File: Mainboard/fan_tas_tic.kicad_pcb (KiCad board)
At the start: 2 copper layers, 155 x 175 mm, 125 parts, among them J1 Ti_Booster_40_J1, P1 CONN_01X04, P10 CONN_01X08, P11 CONN_01X04, P12 CONN_01X04, P13 CONN_01X04, P14 CONN_01X04, P2 CONN_01X04, P3 CONN_01X04, P4 CONN_01X04, P5 CONN_01X04, P6 CONN_01X08, P7 CONN_01X08, P8 CONN_01X08, P9 CONN_01X08, Q1 IRL640, Q10 IRL640, Q11 IRL640, Q12 IRL640, Q13 BSS138, Q14 BSS138, Q15 BSS138, Q16 BSS138, Q17 BSS138, Q18 BSS138, Q19 BSS138, Q2 IRL640, Q20 BSS138, Q3 IRL640, Q4 IRL640, Q5 IRL640, Q6 IRL640, Q7 IRL640, Q8 IRL640, Q9 IRL640, U1 7812, U2 7805, U3 UCC27524, U4 UCC27524, U5 TPIC6B595, U6 PCF8574

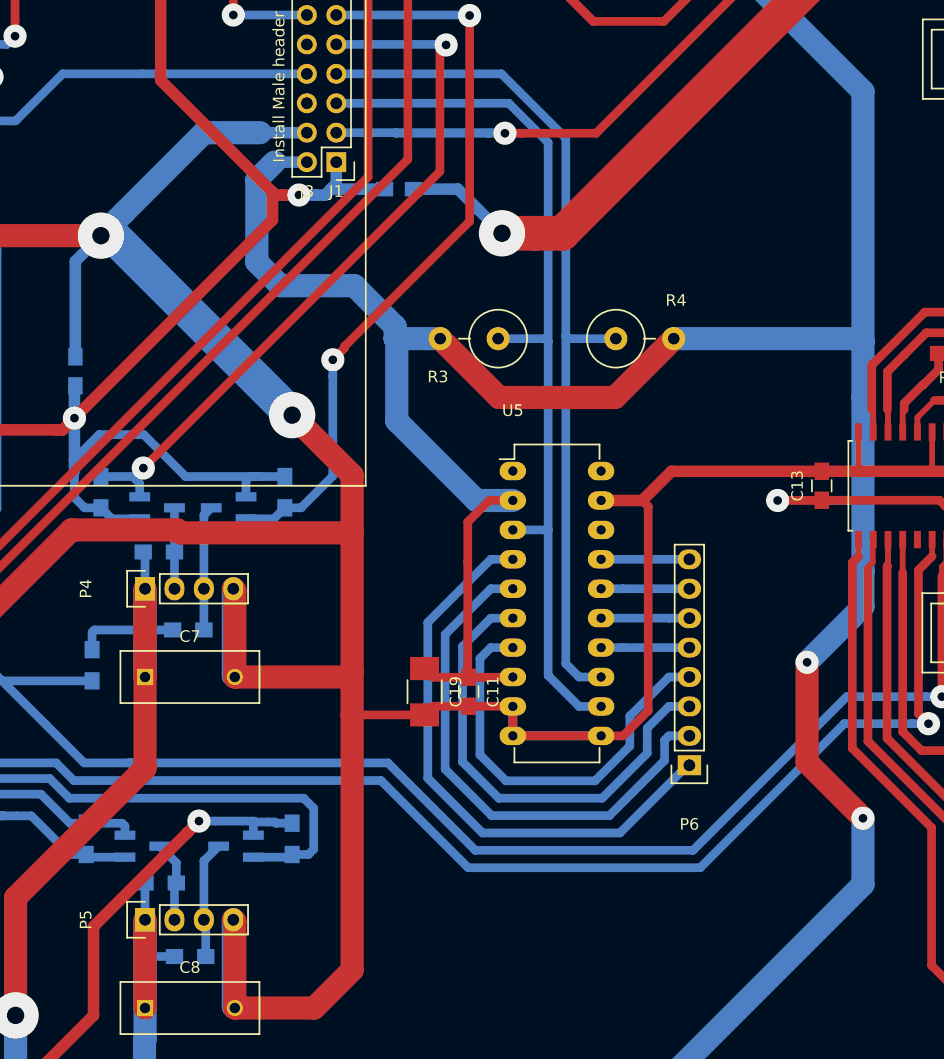
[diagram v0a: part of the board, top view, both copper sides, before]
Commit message: Made space for TM4C123 USB connector
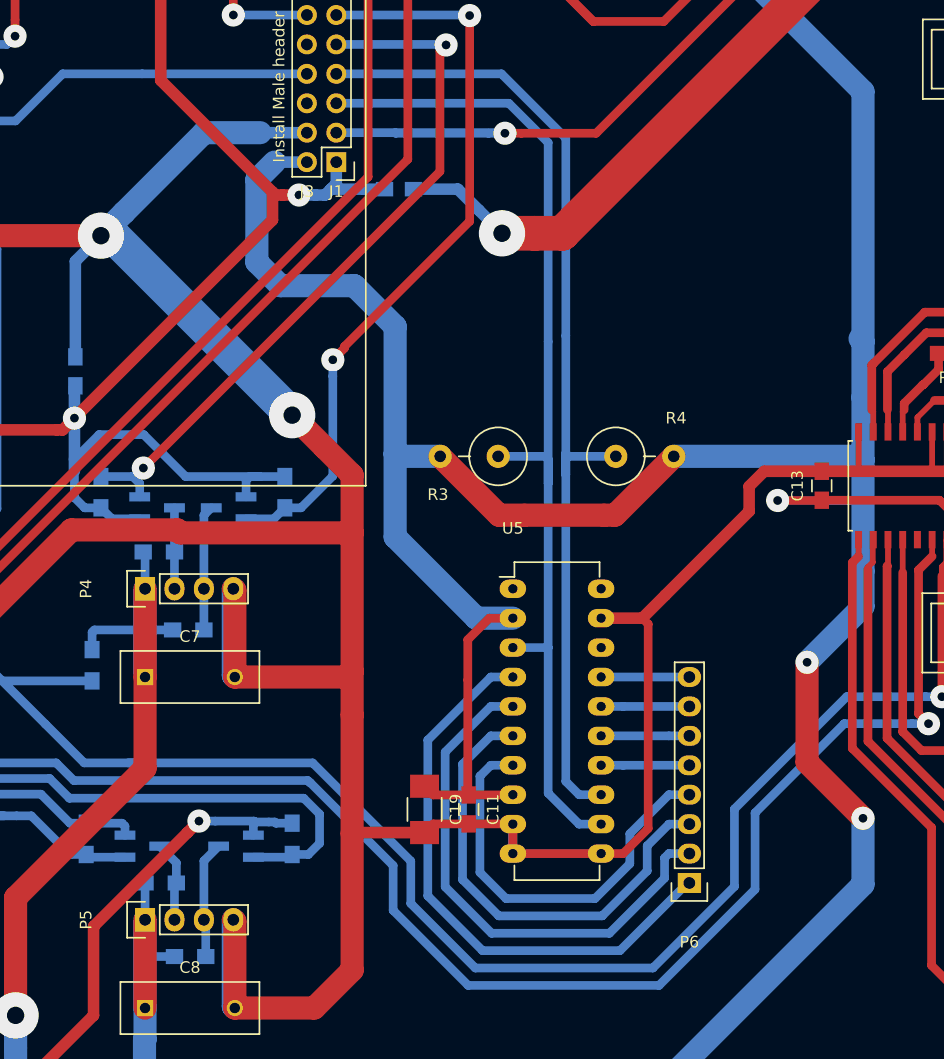
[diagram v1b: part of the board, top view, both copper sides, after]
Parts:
- moved U5 10.2 mm to (88.8, 137.6)
- moved C11 10.2 mm to (85.0, 156.7)
- moved C19 10.2 mm to (81.2, 156.7)
- moved P6 10.2 mm to (104.1, 163.0)
- moved R3 10.2 mm to (85.1, 126.2)
- moved R4 10.2 mm to (100.2, 126.2)
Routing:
- net /I2C_LEVEL_SHIFT0/A_5V: track 135.0 -> 149.6 mm
- net /I2C_LEVEL_SHIFT0/B_5V: track 140.4 -> 154.8 mm
- net /TiviaBoard/sm_col_dat: track 79.2 -> 91.4 mm
- net /TiviaBoard/sm_col_clk: track 75.8 -> 87.8 mm
- net +5V: track 690.9 -> 701.6 mm
- net GND: track 1153.4 -> 1158.9 mm

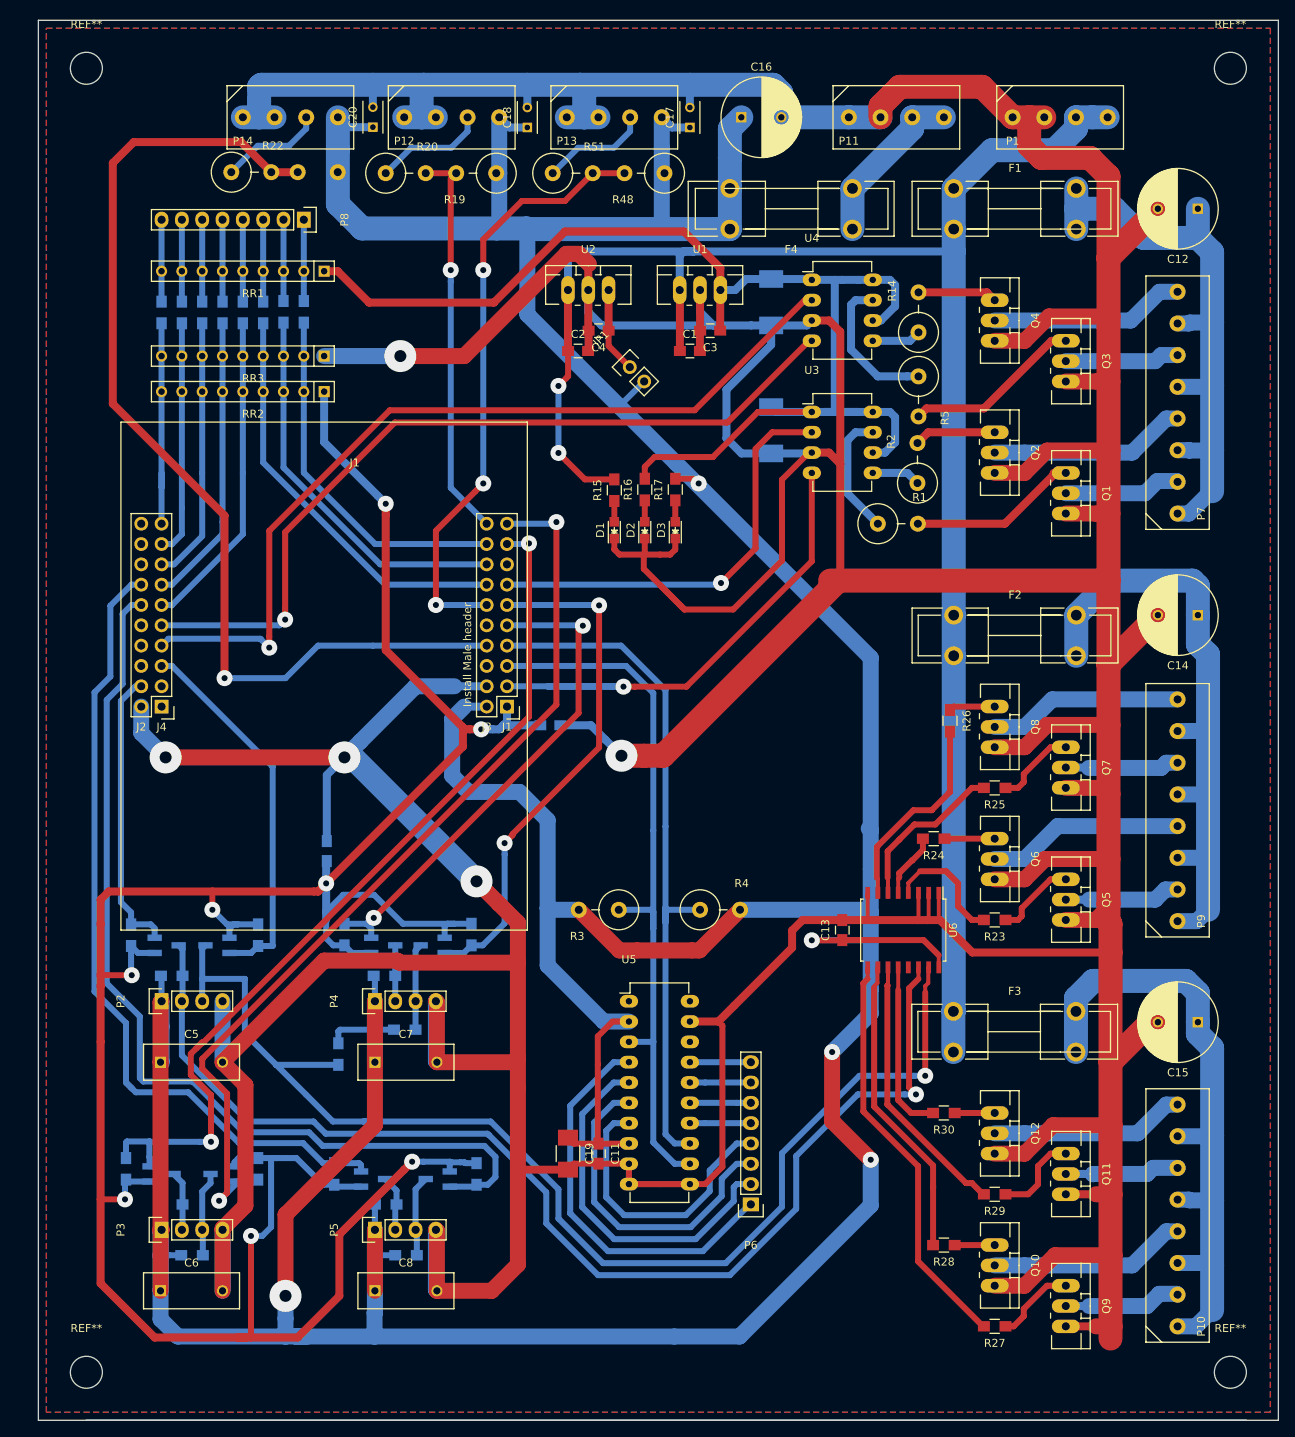
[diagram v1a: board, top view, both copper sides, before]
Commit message: Still Missing WS2811 level shifter
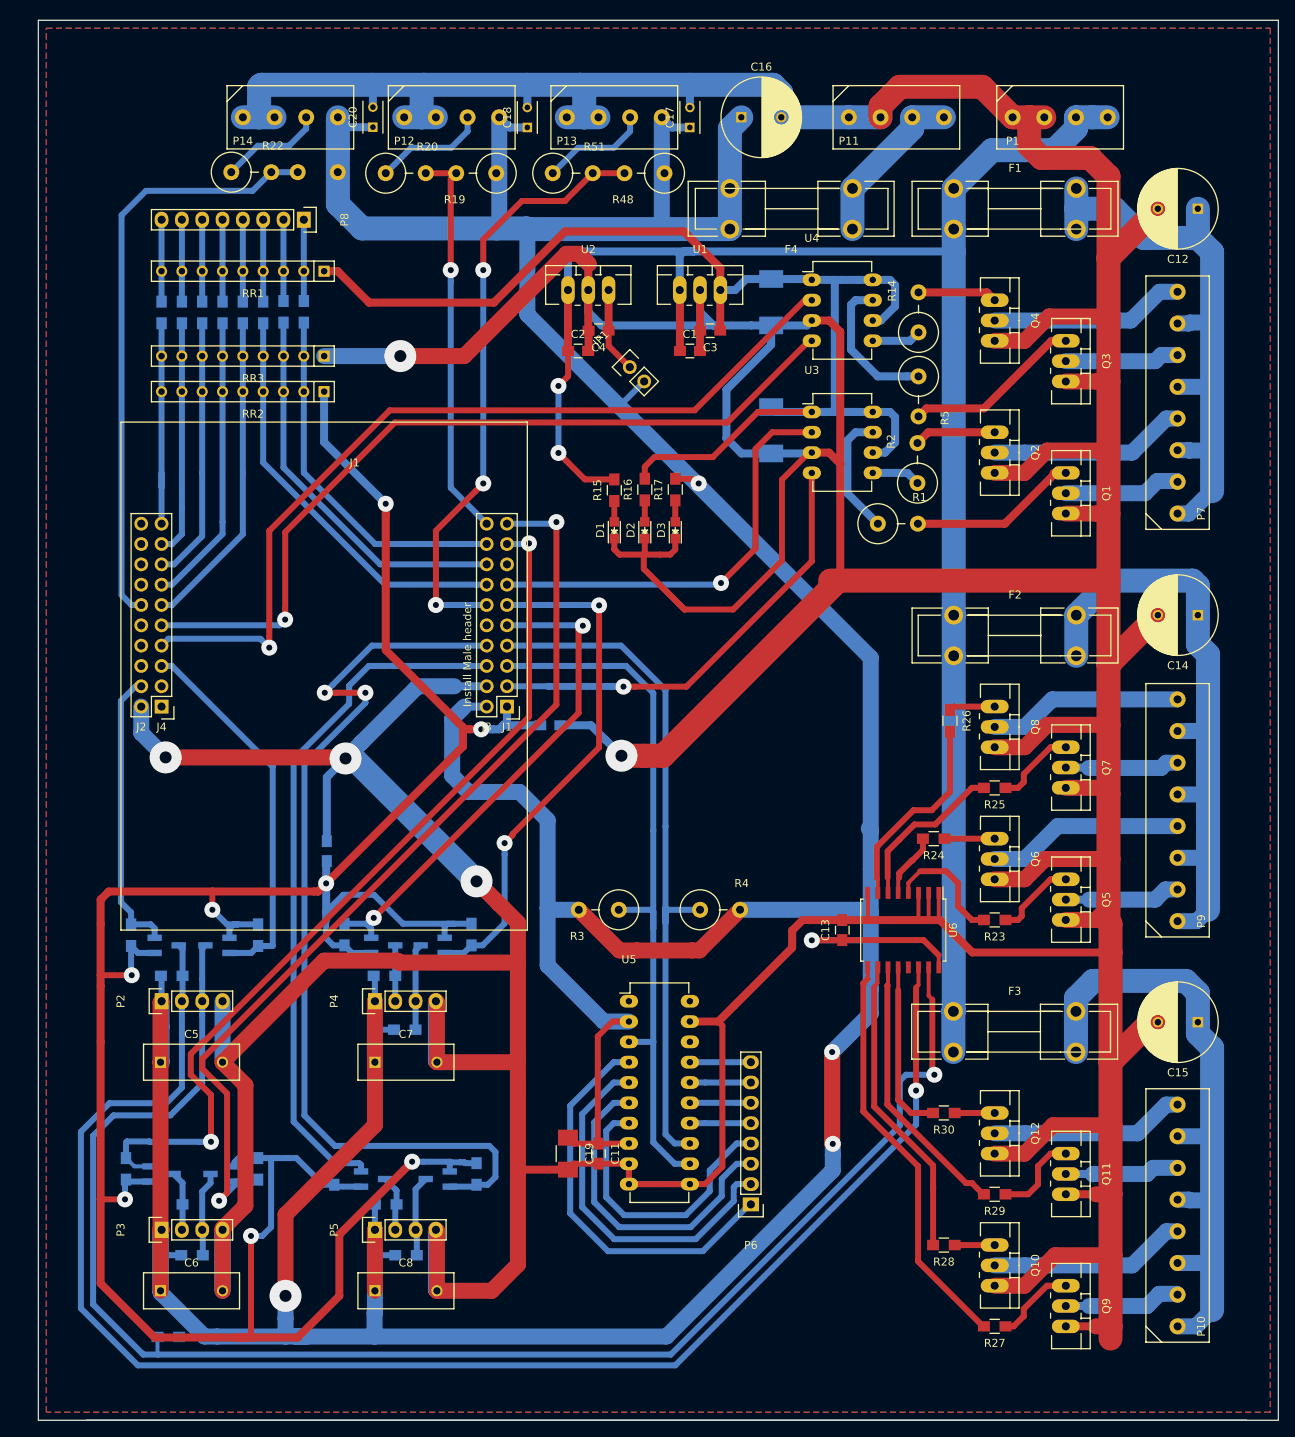
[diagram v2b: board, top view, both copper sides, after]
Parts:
- removed REF** (x4): MountingHole_4mm, Mounting_Holes:MountingHole_4mm
- J1: value Ti_Booster_40_J1 -> Ti_Booster_40
- moved R34 41.3 mm to (31.2, 179.6), turned to 180 degrees
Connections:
- J1 pad 13: Net-(J1-Pad13) -> (no net)
- J1 pad 14: Net-(J1-Pad14) -> (no net)
- J1 pad 15: Net-(J1-Pad15) -> (no net)
- J1 pad 16: /I2C_LEVEL_SHIFT3/B_3V3 -> /TiviaBoard/SSI_2_TX
- J1 pad 17: /I2C_LEVEL_SHIFT3/A_3V3 -> (no net)
- J1 pad 18: /TiviaBoard/SSI_0_RX -> (no net)
- J1 pad 19: /TiviaBoard/SSI_0_/SS -> (no net)
- J1 pad 20: /TiviaBoard/SSI_0_CLK -> (no net)
- J1 pad 23: Net-(J1-Pad23) -> /I2C_LEVEL_SHIFT3/A_3V3
- J1 pad 24: /TiviaBoard/SSI_2_TX -> /I2C_LEVEL_SHIFT3/B_3V3
- J1 pad 25: Net-(J1-Pad25) -> (no net)
- J1 pad 31: Net-(J1-Pad31) -> (no net)
- J1 pad 32: Net-(J1-Pad32) -> (no net)
- J1 pad 8: /TiviaBoard/SSI_0_TX -> (no net)
- U5 pad 1: Net-(U5-Pad1) -> (no net)
- U5 pad 18: Net-(U5-Pad18) -> (no net)
- U5 pad 20: Net-(U5-Pad20) -> (no net)
- U6 pad 13: Net-(U6-Pad13) -> (no net)
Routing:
- net /TiviaBoard/SSI_2_TX: track 130.4 -> 74.7 mm, vias 1 -> 0
- net /I2C_LEVEL_SHIFT0/A_5V: track 149.6 -> 194.8 mm
- net /I2C_LEVEL_SHIFT0/B_5V: track 154.8 -> 196.9 mm
- net /I2C_LEVEL_SHIFT3/A_3V3: track 102.6 -> 87.2 mm
- net +5V: track 701.6 -> 687.4 mm
- net /I2C_LEVEL_SHIFT3/B_3V3: track 120.6 -> 118.9 mm, vias 0 -> 2

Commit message: Added 74HC04 buffer to WS2811 outputs
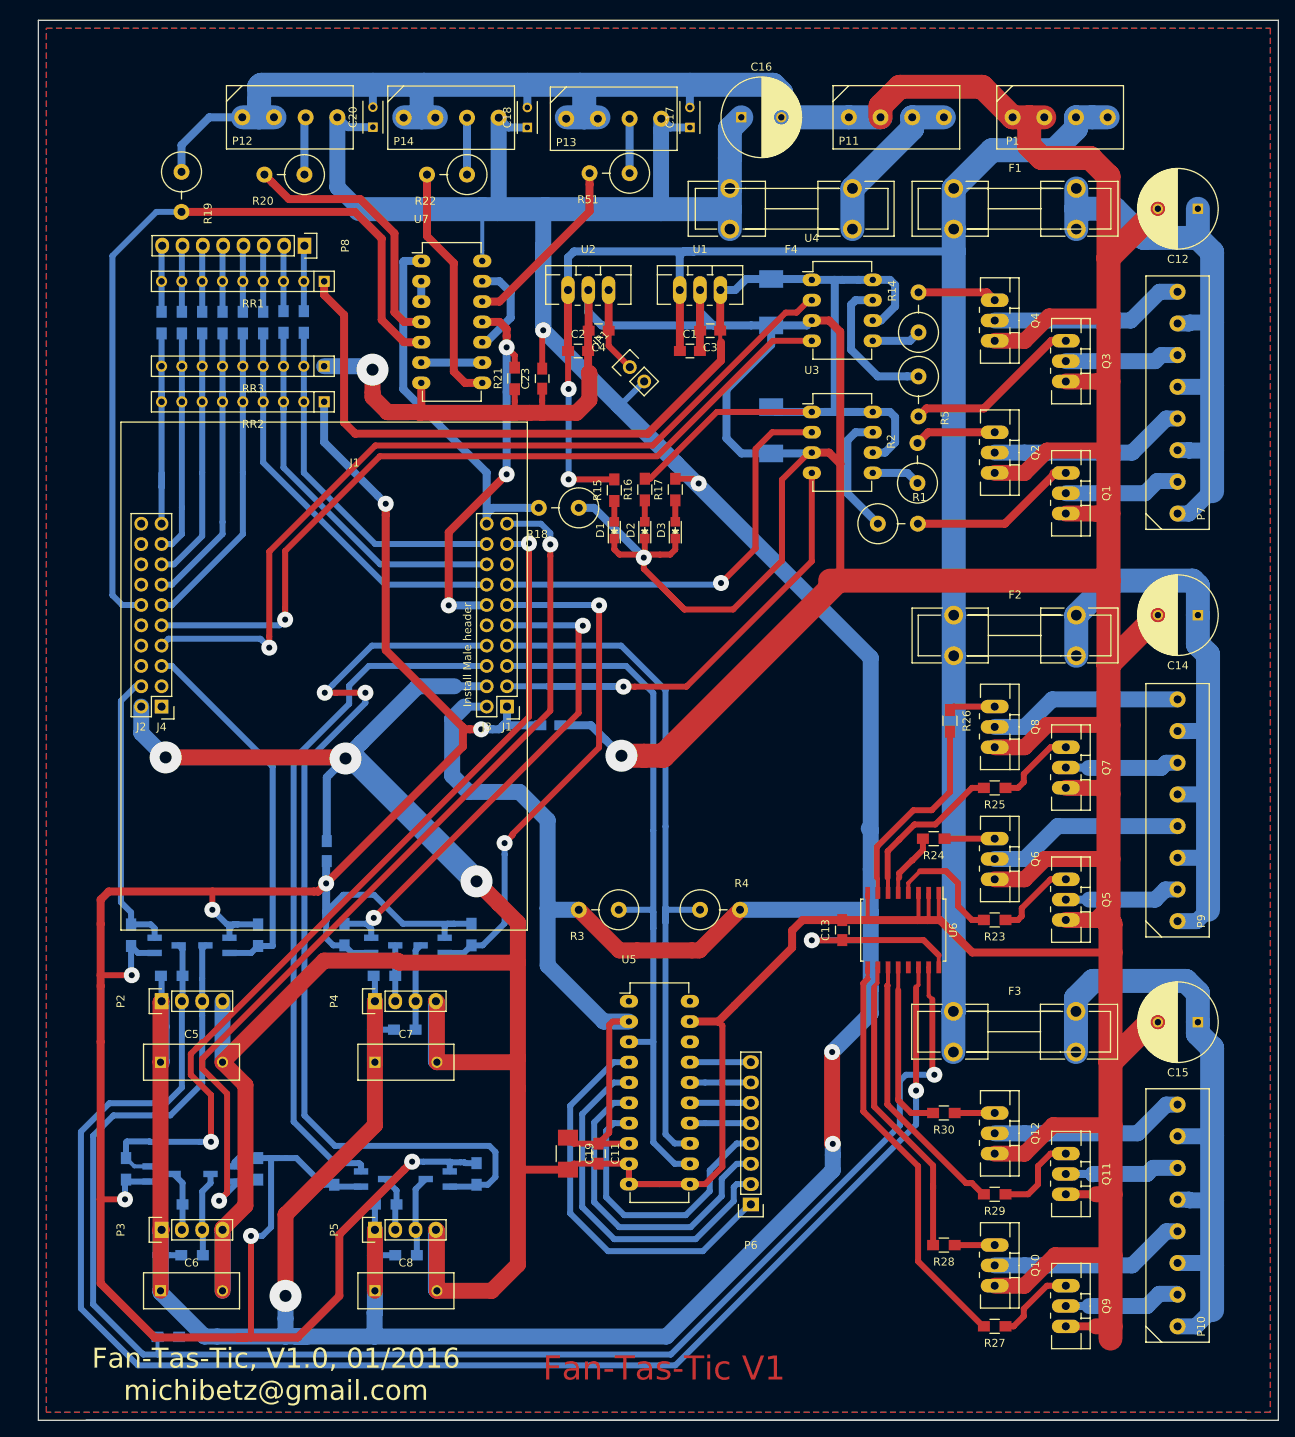
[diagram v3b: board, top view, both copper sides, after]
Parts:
- removed R48: NC, Resistors_ThroughHole:Resistor_Vertical_RM5mm
- added C23: 100nF, Capacitors_SMD:C_0805_HandSoldering, F.Cu at (78.0, 59.8)
- added R18: 4k7, Resistors_ThroughHole:Resistor_Vertical_RM5mm, F.Cu at (80.1, 75.9)
- added U7: 74HC04, Housings_DIP:DIP-14_W7.62mm_LongPads, F.Cu at (62.9, 45.1)
- R19: value NC -> 4k7
- R21: value NC -> 4k7; footprint Resistors_ThroughHole:Resistor_Vertical_RM5mm -> Resistors_SMD:R_0805_HandSoldering; moved to F.Cu
- moved R19 36.9 mm to (32.9, 36.4), turned to 270 degrees
- moved R21 35.7 mm to (74.5, 59.8), turned to 90 degrees
- moved R22 24.5 mm to (66.1, 34.3), turned to 180 degrees
- moved P12 20.2 mm to (40.5, 31.1)
- moved P14 20.1 mm to (60.7, 31.1)
- moved R20 15.2 mm to (45.8, 34.3), turned to 180 degrees
- moved R51 4.61 mm to (86.4, 34.1), turned to 180 degrees
- moved P8 3.25 mm to (48.3, 43.2)
- moved R6 1.27 mm to (48.2, 52.7)
- moved R7 1.27 mm to (45.6, 52.7)
- moved RR1 1.27 mm to (40.6, 47.6)
- moved R10 1.27 mm to (38.0, 52.8)
- moved R11 1.27 mm to (35.5, 52.8)
- moved R12 1.27 mm to (32.9, 52.8)
- moved R13 1.27 mm to (30.4, 52.8)
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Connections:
- R19 pad 1: +5V -> GND
- R19 pad 2: /TiviaBoard/SSI_1_TX -> /TiviaBoard/SSI_2_TX
- R20 pad 2: /TiviaBoard/SSI_1_TX -> Net-(R20-Pad2)
- R21 pad 1: +5V -> GND
- R21 pad 2: /TiviaBoard/SSI_2_TX -> /TiviaBoard/SSI_3_TX
- R22 pad 2: /TiviaBoard/SSI_2_TX -> Net-(R22-Pad2)
- R51 pad 2: /TiviaBoard/SSI_3_TX -> Net-(R51-Pad2)
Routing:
- net GND: track 1158.8 -> 1197.9 mm, vias 5 -> 6
- net Net-(R20-Pad2): track 0.00 -> 33.4 mm
- net Net-(R22-Pad2): track 0.00 -> 30.2 mm
- net /TiviaBoard/SSI_3_TX: track 75.6 -> 48.7 mm
- net /TiviaBoard/SSI_2_TX: track 74.7 -> 100.1 mm
- net Net-(R51-Pad2): track 0.00 -> 22.9 mm
- net +12V: track 161.8 -> 175.4 mm
- net Net-(U7-Pad10): track 0.00 -> 12.1 mm
- net +5V: track 687.4 -> 697.0 mm, vias 5 -> 6
- net Net-(U7-Pad6): track 0.00 -> 7.62 mm
- net Net-(P13-Pad3): track 13.6 -> 6.81 mm
- net Net-(P12-Pad3): track 14.2 -> 7.70 mm
- net Net-(P14-Pad3): track 13.5 -> 7.11 mm
- net /TiviaBoard/SSI_1_TX: track 49.8 -> 46.2 mm, vias 1 -> 0
- net Net-(U7-Pad2): track 0.00 -> 2.54 mm
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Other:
- board text added: "Fan-Tas-Tic V1"
- board text added: "Fan-Tas-Tic, V1.0, 01/2016 michibetz@gmail.com"
